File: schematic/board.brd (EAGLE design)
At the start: 100 x 80 mm, 14 parts, among them U1 STM32F103C8T6, X1 NX3215SA-32.768K, X2 NX5032GA-8MHz

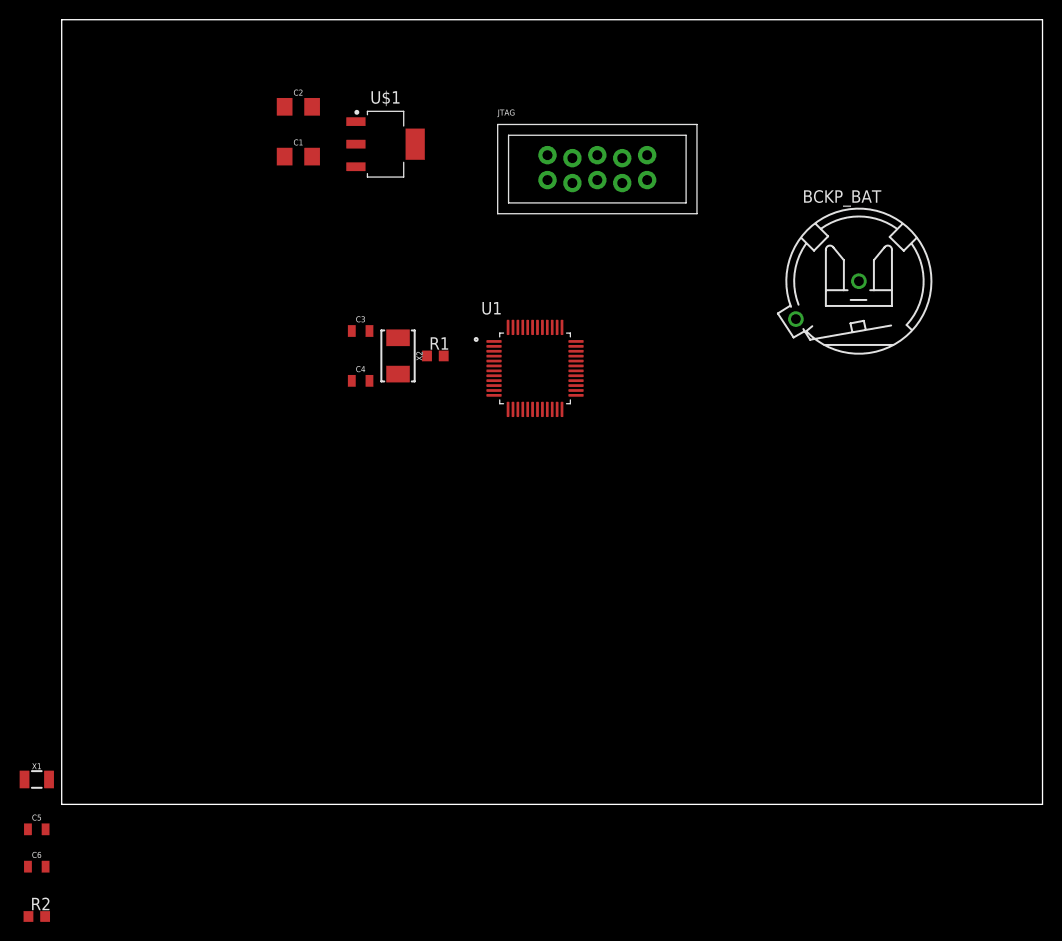
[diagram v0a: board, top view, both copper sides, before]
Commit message: Начерно набросана обвязка мк (без фильтрующих кондеров). Обвязка МК нагло срисована с блюпила без номиналов
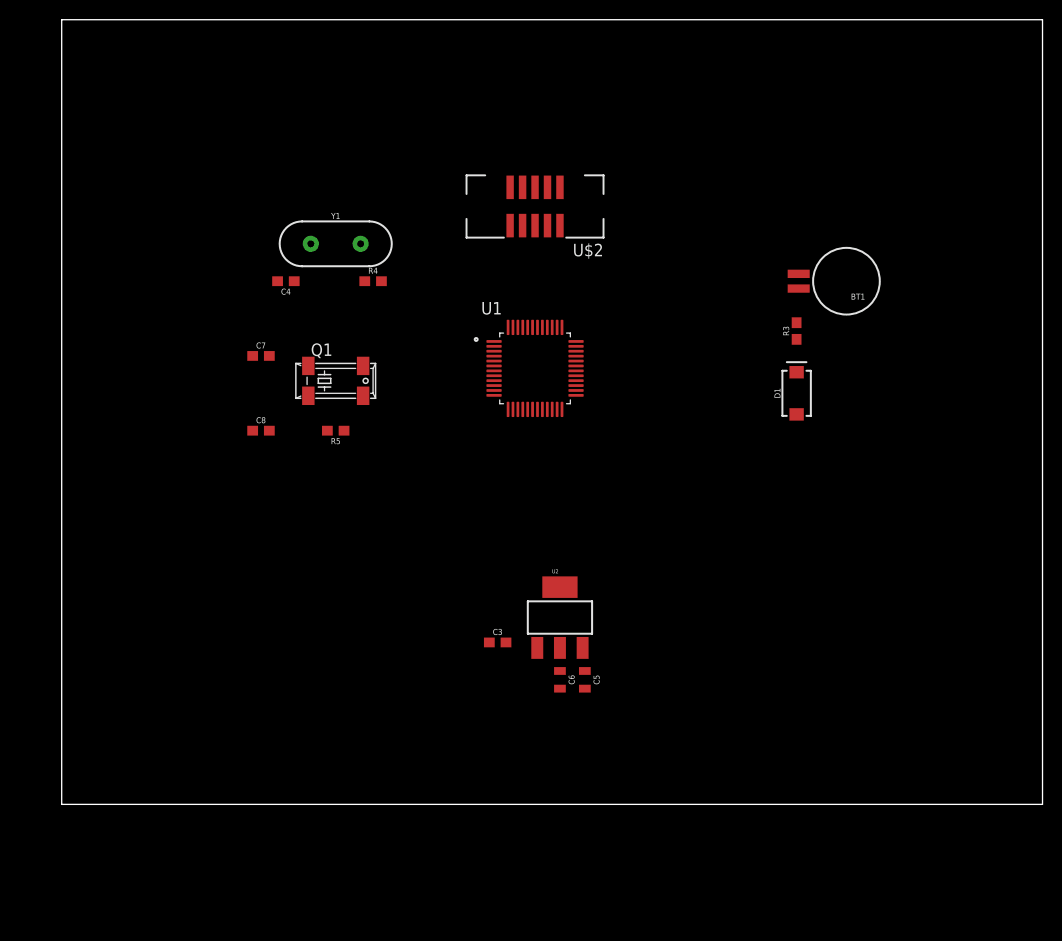
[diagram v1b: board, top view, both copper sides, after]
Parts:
- removed BCKP_BAT: CH23-1220LF, battery:CH23-1220LF
- removed C1: 10uF, SparkFun-Capacitors:1206
- removed C2: 100uF, SparkFun-Capacitors:1206
- removed JTAG: DS-1013-10LOCK, IDC:DS1013-10-LOCK
- removed R1: 1.5kOhm, rcl:R0603
- removed R2: 0 Ohm, rcl:R0603
- removed U$1: LD1117AS33TR, VREG:SOT230P700X180-4
- removed X1: NX3215SA-32.768K, SparkFun-Clocks:CRYSTAL-SMD-3.2X1.5MM
- removed X2: NX5032GA-8MHz, SparkFun-Clocks:CRYSTAL-SMD-5X3.2-2PAD
- added BT1: 6.8MM_COIN_CELL, SparkFun-Batteries:BATTCON-6.8MM
- added C7, C8: 4.7uF, SparkFun-Capacitors:0603
- added D1: 1A/40V/500mV, SparkFun-DiscreteSemi:SMA-DIODE
- added Q1: (no value), crystal:MM20SS
- added R3, R4, R5: (no value), SparkFun-Resistors:0603
- added U$2: CST2-JTAG, IDC:2X5-1.27MM-SMT
- added U2: (no value), SparkFun-IC-Power:SOT223
- added Y1: (no value), SparkFun-Clocks:HC49US
- C3, C4: value 8uF -> 4.7uF; device SparkFun-Capacitors:0805 -> SparkFun-Capacitors:0603
- C5, C6: value 7uF -> 1.0uF
- moved C5 57.9 mm to (53.3, 12.7), turned to 270 degrees
- moved C6 56.6 mm to (50.8, 12.7), turned to 270 degrees
- moved C3 34.7 mm to (44.5, 16.5)
- moved C4 12.7 mm to (22.9, 53.3), turned to 180 degrees
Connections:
- new net N$7: D1.C, R3.2
- net +3V3: now also C5.1, D1.A, U$2.1, U2.3; no longer C1.1, JTAG.1, U$1.3
- net +5V: now also C6.1, U$2.3, U2.2, U2.4; no longer C2.1, JTAG.3, U$1.2, U$1.4
- net GND: now also BT1.-, C3.2, C4.2, C7.1, C8.1, U$2.9, U2.1; no longer BCKP_BAT.-, C1.2, C2.2, C3.1, C4.1, JTAG.9, U$1.1
- net JTCK: now also U$2.4; no longer JTAG.4
- net JTDI: now also U$2.8; no longer JTAG.8
- net JTDO: now also U$2.6; no longer JTAG.6
- net JTMS: now also U$2.2; no longer JTAG.2
- net N$1: now also C3.1, Y1.2; no longer C4.2, X2.P$1
- net N$2: now also R4.2; no longer R1.2
- net N$3: now also C8.2, Q1.1, R5.2; no longer C6.1, R2.2, X1.P$1
- net N$4: now also C4.1, R4.1, Y1.1; no longer C3.2, R1.1, X2.P$2
- net N$5: now also C7.2, Q1.4; no longer C5.1, X1.P$2
- net N$6: now also R5.1; no longer R2.1
- net NRST: now also U$2.10; no longer JTAG.10
- net VBAT: now also BT1.+, R3.1; no longer BCKP_BAT.+

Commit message: Радиомодули LORA 433
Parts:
- removed R4, R5: (no value), SparkFun-Resistors:0603
- added R1, R2: (no value), SparkFun-Resistors:0603
- added U$1: E22-400M30S, ebyte-radio:E22-400M30S
- added U$3: E22-400M22S, ebyte-radio:E22-400M22S
- moved C5 12.8 mm to (54.6, 25.4)
- moved C6 12.8 mm to (52.1, 25.4)
- moved U2 12.8 mm to (52.1, 31.8)
- moved C3 9.25 mm to (47.0, 25.4)
- moved C4 2.54 mm to (20.3, 53.3)
- turned U$2 to 0 degrees
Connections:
- removed net N$1: C3.1, U1.5, Y1.2
- removed net N$2: R4.2, U1.6
- removed net N$3: C8.2, Q1.1, R5.2
- removed net N$4: C4.1, R4.1, Y1.1
- removed net N$5: C7.2, Q1.4, U1.3
- removed net N$6: R5.1, U1.4
- new net E22-BUSY: U$1.14, U$3.14
- new net E22-CLK: U$1.18, U$3.18
- new net E22-CS: U$1.19, U$3.19
- new net E22-DIO1: U$1.13, U$3.13
- new net E22-DIO2: U$1.8, U$3.8
- new net E22-MISO: U$1.16, U$3.16
- new net E22-MOSI: U$1.17, U$3.17
- new net E22-NRST: U$1.15, U$3.15
- new net E22-RXEN: U$1.6, U$3.6
- new net E22-TXEN: U$1.7, U$3.7
- new net HSE-IN: C4.1, U1.5, Y1.1
- new net HSE-OUT: R2.2, U1.6
- new net LSE-IN: C8.2, Q1.1, U1.3
- new net LSE-OUT: R1.1, U1.4
- new net N$8: C7.2, Q1.4, R1.2
- new net N$9: C3.1, R2.1, Y1.2
- net +5V: now also U$1.10, U$1.9, U$3.9
- net GND: now also U$1.1, U$1.11, U$1.12, U$1.2, U$1.20, U$1.22, U$1.3, U$1.4, U$1.5, U$3.1, U$3.10, U$3.11, U$3.12, U$3.2, U$3.20, U$3.22, U$3.3, U$3.4, U$3.5

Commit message: Модули для NRF24 в каком-то виде на платах
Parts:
- added U$4: E01-ML01SP4, ebyte-radio:E01-ML01SP4
- added U$5: E01-ML01DP5, ebyte-radio:E01-ML01DP5/E01-2G4M27D
- moved BT1 72.2 mm to (16.5, 19.1), turned to 90 degrees
- moved R3 62.7 mm to (15.2, 29.2)
- moved D1 57.8 mm to (17.8, 33.0), turned to 180 degrees
- moved C3 47.4 mm to (30.5, 69.8), flipped to the bottom, turned to 180 degrees
- moved R2 38.6 mm to (34.3, 66.0)
- moved U$2 32.8 mm to (29.2, 34.3)
- moved C6 28.1 mm to (25.4, 16.5)
- moved U2 25.6 mm to (29.2, 20.3), turned to 180 degrees
- moved C5 25.4 mm to (29.2, 26.7), turned to 0 degrees
- moved U1 24.4 mm to (26.7, 55.9), turned to 270 degrees
- moved U$1 23.3 mm to (57.1, 26.7)
- moved U$3 23.3 mm to (57.1, 26.7)
- moved Q1 18.9 mm to (14.0, 55.9), turned to 90 degrees
- moved C8 18.2 mm to (16.5, 55.9), flipped to the bottom, turned to 270 degrees
- moved C4 16.7 mm to (22.9, 69.8), flipped to the bottom, turned to 0 degrees
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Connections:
- new net VCC: U$4.1, U$5.2
- net GND: now also U$4.10, U$4.8, U$4.9, U$5.1
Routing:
- added copper zone on layer 1, net GND
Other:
- board size 100 x 80 mm -> 80 x 80 mm

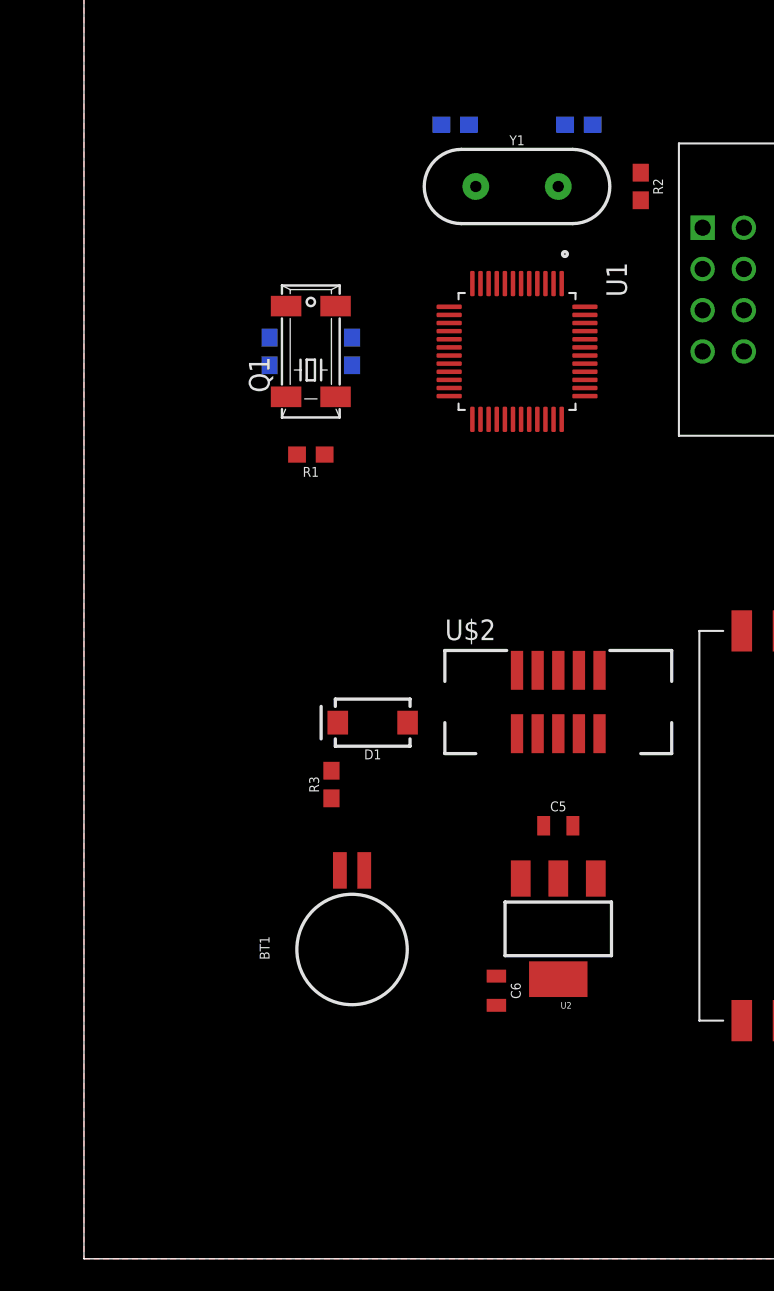
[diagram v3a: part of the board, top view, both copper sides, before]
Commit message: Новый вариант разъема для отладки
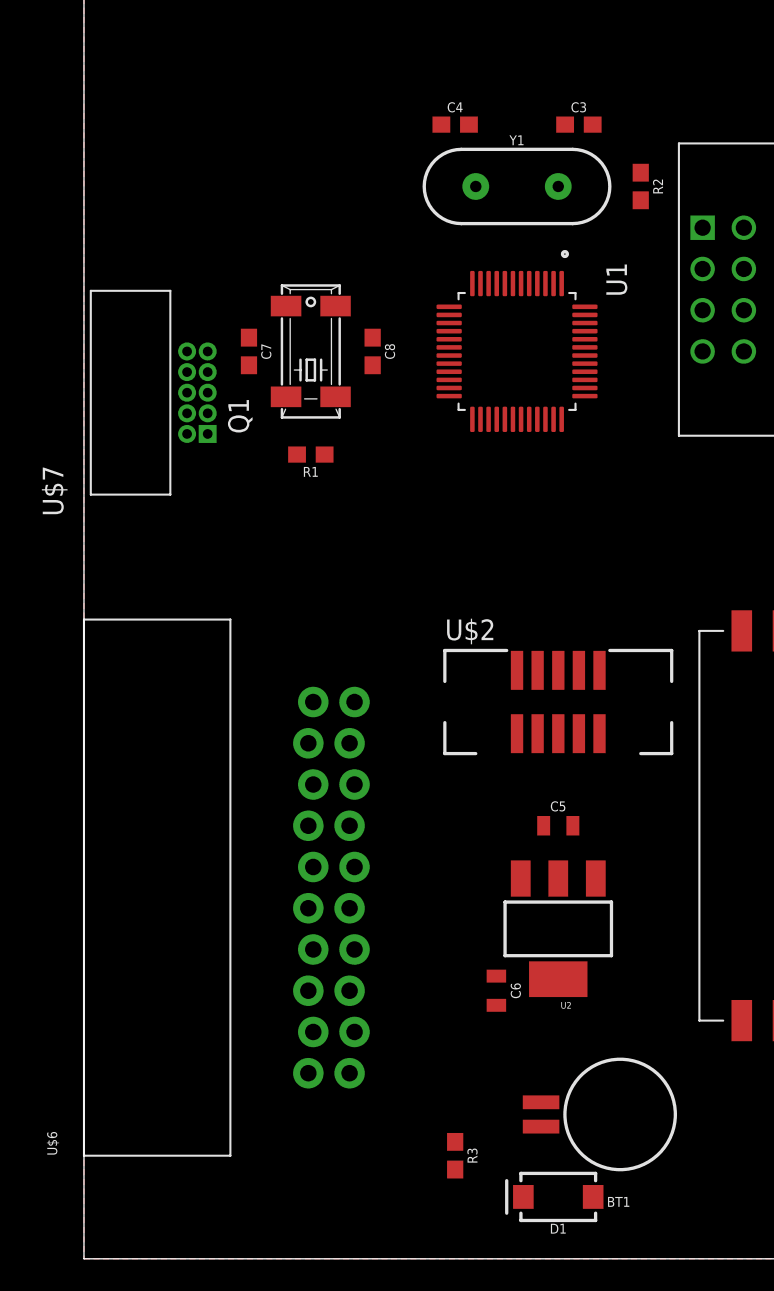
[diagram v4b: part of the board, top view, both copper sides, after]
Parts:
- added U$6: DS-1013-20LOCK, IDC:DS1013-20R-LOCK
- added U$7: CST2-JTAG2X5-1.27MM-R, IDC:2X5-1.27MM-R
- moved D1 31.4 mm to (29.2, 3.81)
- moved R3 24.1 mm to (22.9, 6.35), turned to 270 degrees
- moved BT1 19.4 mm to (33.0, 8.89), turned to 180 degrees
- moved C7 1.27 mm to (10.2, 55.9), flipped to the top
- moved C8 1.27 mm to (17.8, 55.9), flipped to the top
- flipped C3 to the top, turned to 0 degrees
- flipped C4 to the top

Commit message: Прикидки размеров платы
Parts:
- removed U$5: E01-ML01DP5, ebyte-radio:E01-ML01DP5/E01-2G4M27D
- removed U$7: CST2-JTAG2X5-1.27MM-R, IDC:2X5-1.27MM-R
- added J1: (no value), SparkFun-Connectors:2X4
- added P1: S8B-PH-K, con-jst-ph:S8B-PH-K
- U$2: value CST2-JTAG -> TFP09-2-12B; device IDC:2X5-1.27MM-SMT -> sdcard:TFP09-2-12B
- moved BT1 41.2 mm to (19.1, 47.6), flipped to the bottom, turned to 270 degrees
- moved D1 35.5 mm to (22.9, 38.7), flipped to the bottom, turned to 90 degrees
- moved U$2 33.9 mm to (33.0, 67.9), flipped to the bottom, turned to 180 degrees
- moved R3 33.8 mm to (15.9, 39.4), flipped to the bottom
- moved R1 25.8 mm to (34.3, 65.4), turned to 90 degrees
- moved U$6 18.9 mm to (27.3, 37.5)
- moved C4 18.8 mm to (15.2, 52.7), flipped to the bottom
- moved C3 17.0 mm to (15.2, 62.2), flipped to the bottom
- moved C6 15.3 mm to (19.1, 30.5), flipped to the bottom, turned to 180 degrees
- moved Y1 13.1 mm to (16.5, 57.8), flipped to the bottom, turned to 90 degrees
- moved C7 12.9 mm to (22.2, 60.3), flipped to the bottom
- moved U2 11.4 mm to (19.1, 25.4), flipped to the bottom, turned to 270 degrees
- moved U$1 9.52 mm to (51.4, 34.3)
- moved U$3 9.52 mm to (51.4, 34.3)
- moved Q1 8.47 mm to (22.2, 57.8)
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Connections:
- net +3V3: no longer U$2.1
- net +5V: no longer U$2.3
- net GND: no longer U$2.9, U$5.1
- net JTCK: no longer U$2.4
- net JTDI: no longer U$2.8
- net JTDO: no longer U$2.6
- net JTMS: no longer U$2.2
- net NRST: no longer U$2.10
- net VCC: no longer U$5.2
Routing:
- removed copper zone on layer 1, net GND
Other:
- board size 80 x 80 mm -> 60 x 60 mm

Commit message: Замороженное состояние
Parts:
- removed U$6: DS-1013-20LOCK, IDC:DS1013-20R-LOCK
- added U3: LSM6DS3, LSM6DS3:PQFN50P300X250X86-14N
- added U4: LSM303CTR, LSM303CTR:LGA12R50P_200X200X100
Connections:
- new net VDD: U3.8, U4.9
- new net VDDIO: U3.5
- new net VDD_IO: U4.10
- net GND: now also U3.6, U3.7, U4.6, U4.8
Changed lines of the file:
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@@
 </class>
 </classes>
-<designrules name="default">
+<designrules name="default *">
 <description language="de">&lt;b&gt;EAGLE Design Rules&lt;/b&gt;
 &lt;p&gt;
@@
 necessary adjustments and save your customized
 design rules under a new name.</description>
-<param name="layerSetup" value="(1*16)"/>
+<param name="layerSetup" value="(1+2*15+16)"/>
 <param name="mtCopper" value="0.035mm 0.035mm 0.035mm 0.035mm 0.035mm 0.035mm 0.035mm 0.035mm 0.035mm 0.035mm 0.035mm 0.035mm 0.035mm 0.035mm 0.035mm 0.035mm"/>
 <param name="mtIsolate" value="1.5mm 0.15mm 0.2mm 0.15mm 0.2mm 0.15mm 0.2mm 0.15mm 0.2mm 0.15mm 0.2mm 0.15mm 0.2mm 0.15mm 0.2mm"/>
@@
 <attribute name="VALUE" x="57.785" y="67.31" size="1.27" layer="27" rot="R180"/>
 </element>
-<element name="U$6" library="IDC" package="DS1013-20R-LOCK" value="DS-1013-20LOCK" x="27.305" y="37.465" smashed="yes" rot="R90">
-<attribute name="NAME" x="10.414" y="20.955" size="0.6096" layer="25" font="vector" ratio="20" rot="R90"/>
-<attribute name="VALUE" x="31.115" y="20.955" size="0.6096" layer="27" font="vector" ratio="20" rot="R90"/>
-</element>
 <element name="J1" library="SparkFun-Connectors" package="2X4" value="" x="66.04" y="57.15" smashed="yes" rot="R90">
 <attribute name="NAME" x="63.246" y="52.07" size="0.6096" layer="25" font="vector" ratio="20" rot="R90"/>
@@
 <attribute name="NAME" x="28.702" y="20.701" size="1.016" layer="25" ratio="18"/>
 <attribute name="VALUE" x="24.36" y="14.005" size="1.016" layer="27" ratio="10" rot="R90"/>
+</element>
+<element name="U3" library="LSM6DS3" package="PQFN50P300X250X86-14N" value="LSM6DS3" x="15.875" y="7.62" smashed="yes">
+<attribute name="AVAILABILITY" value="Unavailable" x="15.875" y="7.62" size="1.778" layer="27" display="off"/>
+<attribute name="DESCRIPTION" value=" iNEMO inertial module: 3D accelerometer and 3D gyroscope " x="15.875" y="7.62" size="1.778" layer="27" display="off"/>
+<attribute name="MF" value="STMicroelectronics" x="15.875" y="7.62" size="1.778" layer="27" display="off"/>
+<attribute name="MP" value="LSM6DS3" x="15.875" y="7.62" size="1.778" layer="27" display="off"/>
+<attribute name="NAME" x="13.022090625" y="9.471890625" size="1.2713" layer="25"/>
+<attribute name="PACKAGE" value="LGA-14 STMicroelectronics" x="15.875" y="7.62" size="1.778" layer="27" display="off"/>
+<attribute name="PRICE" value="None" x="15.875" y="7.62" size="1.778" layer="27" display="off"/>
+<attribute name="VALUE" x="13.02443125" y="4.5944" size="1.27025" layer="27"/>
+</element>
+<element name="U4" library="LSM303CTR" package="LGA12R50P_200X200X100" value="LSM303CTR" x="10.16" y="6.35" smashed="yes">
+<attribute name="AVAILABILITY" value="Unavailable" x="10.16" y="6.35" size="1.778" layer="27" display="off"/>
+<attribute name="DESCRIPTION" value=" MEMS Module, Tri-Axis Accelerometer, Tri-Axis Magnetometer, 2g, 4g, 8g, 16g, LGA, 12, 1.9 V " x="10.16" y="6.35" size="1.778" layer="27" display="off"/>
+<attribute name="MF" value="STMicroelectronics" x="10.16" y="6.35" size="1.778" layer="27" display="off"/>
+<attribute name="MP" value="LSM303CTR" x="10.16" y="6.35" size="1.778" layer="27" display="off"/>
+<attribute name="NAME" x="8.906809375" y="7.603190625" size="0.30558125" layer="25"/>
+<attribute name="PACKAGE" value="LGA-12 STMicroelectronics" x="10.16" y="6.35" size="1.778" layer="27" display="off"/>
+<attribute name="PRICE" value="None" x="10.16" y="6.35" size="1.778" layer="27" display="off"/>
+<attribute name="VALUE" x="8.9072" y="4.59608125" size="0.305484375" layer="27"/>
 </element>
 </elements>
@@
 <contactref element="U$4" pad="9"/>
 <contactref element="U$4" pad="8"/>
+<contactref element="U3" pad="7"/>
+<contactref element="U3" pad="6"/>
+<contactref element="U4" pad="8"/>
+<contactref element="U4" pad="6"/>
 <wire x1="56.705" y1="54.98" x2="56.705" y2="69.48" width="0" layer="19" extent="1-1"/>
 <wire x1="60.145" y1="46.29" x2="56.705" y2="54.98" width="0" layer="19" extent="1-1"/>
@@
 <wire x1="32.27" y1="61.33" x2="37.2" y2="59.4" width="0" layer="19" extent="1-1"/>
 <wire x1="28.84" y1="54.9" x2="35.27" y2="52.97" width="0" layer="19" extent="1-1"/>
-<wire x1="22.225" y1="56.095" x2="28.84" y2="54.9" width="0" layer="19" extent="1-1"/>
-<wire x1="22.225" y1="61.175" x2="22.225" y2="56.095" width="0" layer="19" extent="1-1"/>
-<wire x1="14.39" y1="52.705" x2="32.27" y2="61.33" width="0" layer="19" extent="1-1"/>
-<wire x1="14.39" y1="62.23" x2="14.39" y2="52.705" width="0" layer="19" extent="1-1"/>
-<wire x1="43.815" y1="57.79" x2="50.035" y2="46.29" width="0" layer="19" extent="1-1"/>
+<wire x1="22.225" y1="56.095" x2="28.84" y2="54.9" width="0" layer="19" extent="1-16"/>
+<wire x1="22.225" y1="61.175" x2="22.225" y2="56.095" width="0" layer="19" extent="16-16"/>
+<wire x1="43.815" y1="57.79" x2="37.2" y2="59.4" width="0" layer="19" extent="1-1"/>
+<wire x1="14.39" y1="62.23" x2="22.225" y2="61.175" width="0" layer="19" extent="16-16"/>
+<wire x1="14.39" y1="52.705" x2="22.225" y2="56.095" width="0" layer="19" extent="16-16"/>
+<wire x1="19.8" y1="42.755" x2="14.39" y2="52.705" width="0" layer="19" extent="16-16"/>
+<wire x1="19.95" y1="30.48" x2="19.8" y2="42.755" width="0" layer="19" extent="16-16"/>
+<wire x1="22.1488" y1="27.7114" x2="19.95" y2="30.48" width="0" layer="19" extent="16-16"/>
+<wire x1="25.4" y1="21.325" x2="22.1488" y2="27.7114" width="0" layer="19" extent="16-16"/>
+<wire x1="34.795" y1="22.29" x2="25.4" y2="21.325" width="0" layer="19" extent="1-16"/>
+<wire x1="43.435" y1="27.29" x2="34.795" y2="22.29" width="0" layer="19" extent="1-1"/>
 <wire x1="60.435" y1="27.29" x2="60.435" y2="41.26" width="0" layer="19" extent="1-1"/>
 <wire x1="57.895" y1="27.29" x2="60.435" y2="27.29" width="0" layer="19" extent="1-1"/>
 <wire x1="60.145" y1="22.29" x2="60.435" y2="27.29" width="0" layer="19" extent="1-1"/>
 <wire x1="65.225" y1="22.29" x2="60.145" y2="22.29" width="0" layer="19" extent="1-1"/>
-<wire x1="43.435" y1="27.29" x2="43.435" y2="41.26" width="0" layer="19" extent="1-1"/>
-<wire x1="34.795" y1="22.29" x2="43.435" y2="27.29" width="0" layer="19" extent="1-1"/>
-<wire x1="22.1488" y1="27.7114" x2="34.795" y2="22.29" width="0" layer="19" extent="1-1"/>
-<wire x1="25.4" y1="21.325" x2="22.1488" y2="27.7114" width="0" layer="19" extent="1-1"/>
-<wire x1="19.95" y1="30.48" x2="22.1488" y2="27.7114" width="0" layer="19" extent="1-1"/>
-<wire x1="19.8" y1="42.755" x2="19.95" y2="30.48" width="0" layer="19" extent="1-1"/>
+<wire x1="16.375" y1="6.695" x2="25.4" y2="21.325" width="0" layer="19" extent="1-16"/>
+<wire x1="15.875" y1="6.695" x2="16.375" y2="6.695" width="0" layer="19" extent="1-1"/>
+<wire x1="10.92" y1="6.1" x2="15.875" y2="6.695" width="0" layer="19" extent="1-1"/>
+<wire x1="10.41" y1="5.59" x2="10.92" y2="6.1" width="0" layer="19" extent="1-1"/>
 </signal>
 <signal name="VBAT">
@@
 <contactref element="U$4" pad="1"/>
 </signal>
+<signal name="VDDIO">
+<contactref element="U3" pad="5"/>
+</signal>
+<signal name="VDD">
+<contactref element="U3" pad="8"/>
+<contactref element="U4" pad="9"/>
+<wire x1="10.92" y1="6.6" x2="17.05" y2="6.87" width="0" layer="19" extent="1-1"/>
+</signal>
+<signal name="VDD_IO">
+<contactref element="U4" pad="10"/>
+</signal>
 </signals>
